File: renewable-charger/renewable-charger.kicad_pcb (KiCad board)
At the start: 2 copper layers, 150 x 40 mm, 37 parts, among them J1 Solar Input, J2 Wind Output, J3 Output, J4 USB_B_Micro, J5 Battery, M1 Stepper_Motor_bipolar, Q1 P-channel 30V 4A MOSfet, Q2 P-channel 30V 4A MOSfet, U1 CN3791

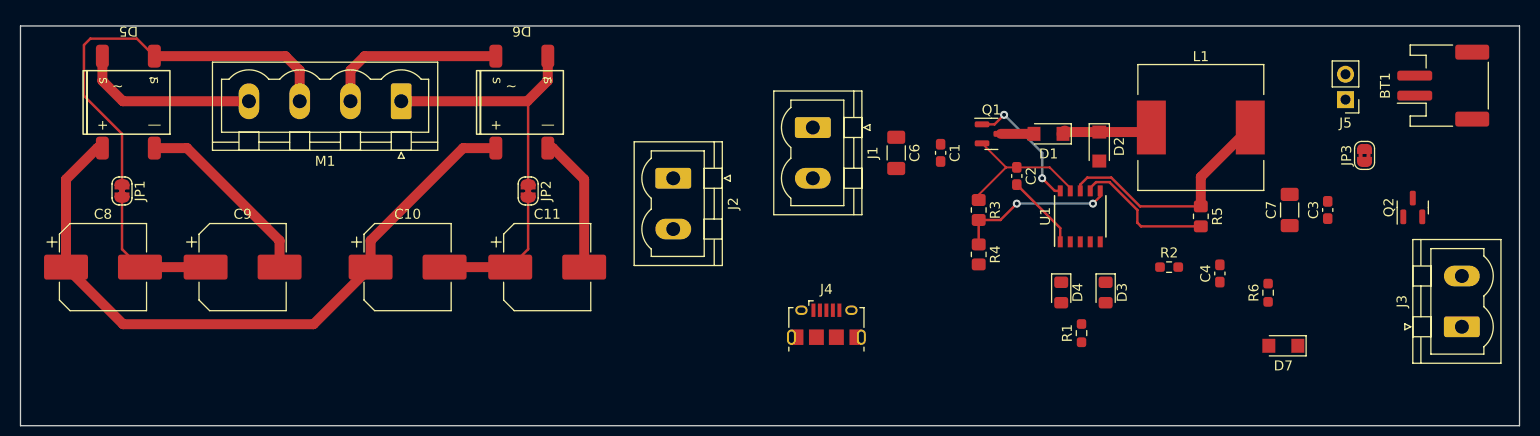
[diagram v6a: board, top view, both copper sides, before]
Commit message: All connections wired on PCB.  Still needs zones, final position for mounting holes and edges, and some labelling.  Part of #4
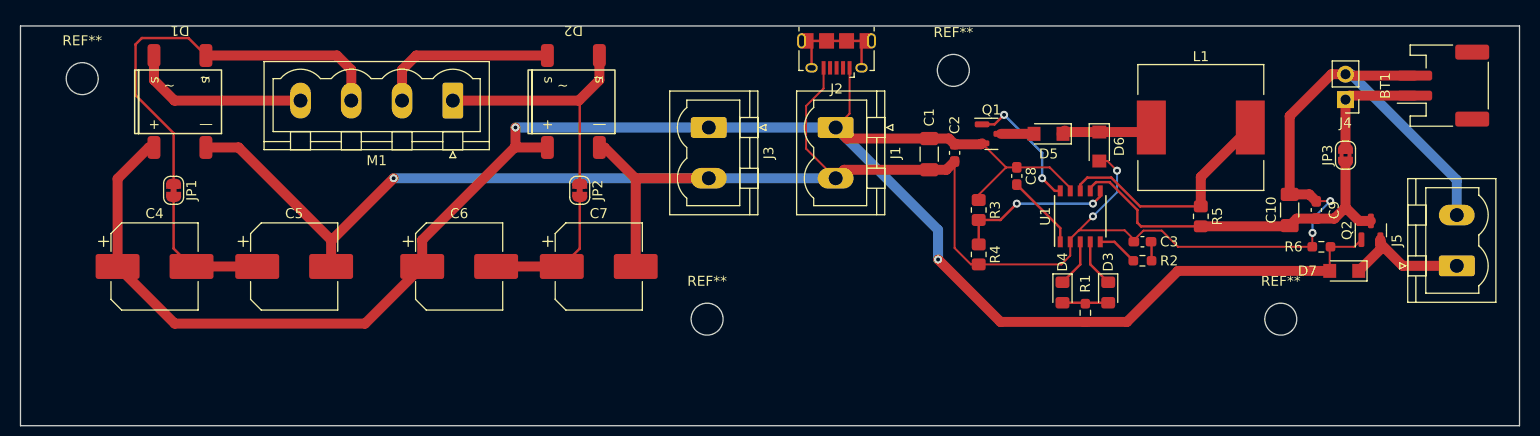
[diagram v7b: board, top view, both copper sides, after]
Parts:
- added REF**: MountingHole_3.2mm_M3_DIN965, MountingHole:MountingHole_3.2mm_M3_DIN965, F.Cu at (205.7, 64.1)
- added REF**: MountingHole_3.2mm_M3_DIN965, MountingHole:MountingHole_3.2mm_M3_DIN965, F.Cu at (181.1, 89.0)
- added REF**: MountingHole_3.2mm_M3_DIN965, MountingHole:MountingHole_3.2mm_M3_DIN965, F.Cu at (118.6, 65.0)
- added REF**: MountingHole_3.2mm_M3_DIN965, MountingHole:MountingHole_3.2mm_M3_DIN965, F.Cu at (238.5, 89.0)
- moved J2 27.1 mm to (194.1, 62.5), turned to 180 degrees
- moved D7 9.66 mm to (244.9, 84.2)
- moved C3 8.37 mm to (224.7, 81.3), turned to 180 degrees
- moved R6 7.04 mm to (242.6, 81.8), turned to 180 degrees
- moved J3 6.20 mm to (181.3, 69.8)
- moved J5 6.12 mm to (256.1, 83.7)
- moved C6 5.16 mm to (156.3, 83.8)
- moved C7 5.16 mm to (170.3, 83.8)
- moved D1 5.16 mm to (128.4, 67.2)
- moved JP2 5.16 mm to (168.4, 76.1)
- moved C4 5.16 mm to (125.8, 83.8)
- moved JP1 5.16 mm to (127.7, 76.1)
- moved C5 5.16 mm to (139.8, 83.8)
- moved D2 5.16 mm to (167.7, 67.2)
- moved M1 5.16 mm to (155.7, 67.2)
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- renumbered C6 to C1, C7 to C10, C1 to C2, C4 to C3, C8 to C4, C9 to C5, C10 to C6, C11 to C7, C2 to C8, C3 to C9, D5 to D1, D6 to D2, D1 to D5, D2 to D6, J4 to J2, J2 to J3, J5 to J4, J3 to J5
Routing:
- net /Power -: track 32.7 -> 229.0 mm, vias 0 -> 5
- net /Power +: track 83.4 -> 206.6 mm, vias 0 -> 2
- net Net-(JP3-A): track 14.2 -> 37.1 mm
- net Net-(D7-K): track 0.00 -> 13.0 mm
- net Net-(BT1-+): track 0.00 -> 12.0 mm
- net unconnected-(J2-Shield): track 0.00 -> 11.5 mm
- net Net-(D3-K): track 0.00 -> 4.79 mm
- net Net-(D4-K): track 0.00 -> 4.78 mm
- net Net-(D3-A): track 0.00 -> 4.65 mm
- net Net-(U1-COM): track 0.00 -> 4.10 mm
- net Net-(C3-Pad1): track 0.00 -> 1.93 mm

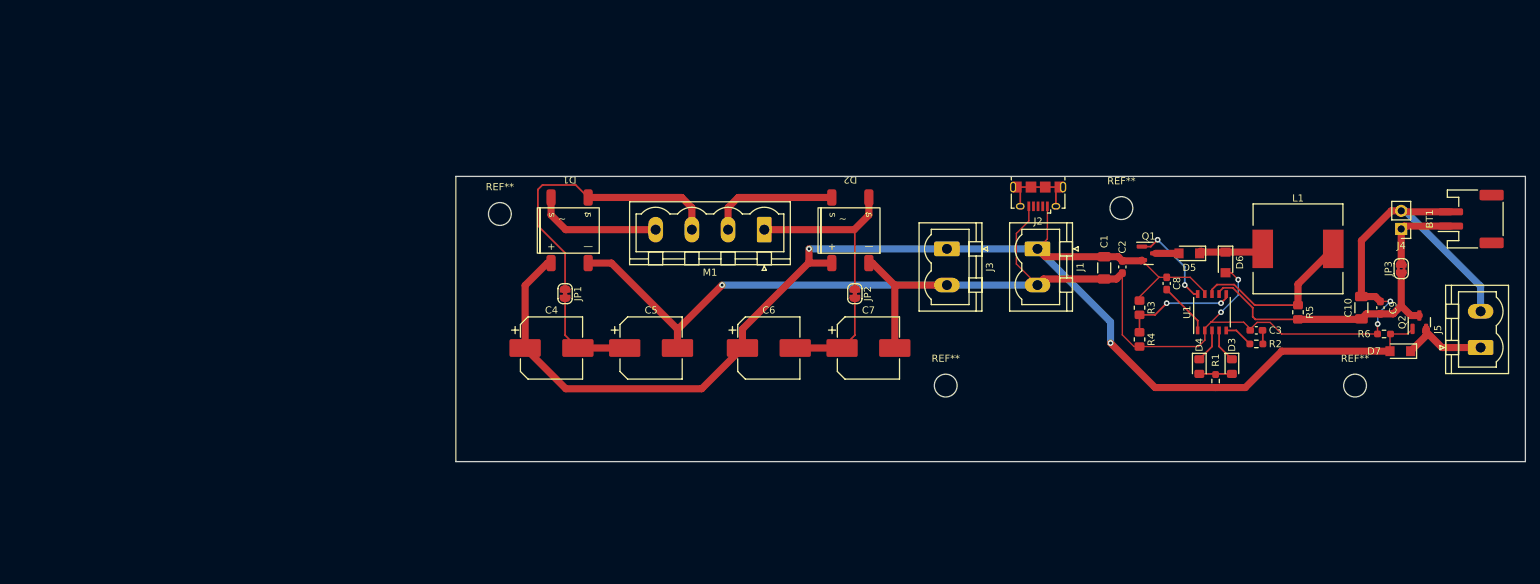
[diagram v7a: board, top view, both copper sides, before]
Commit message: Added copper zones; positioned mounting holes and tidied up edge cuts.  Just labels left.  Part of #4
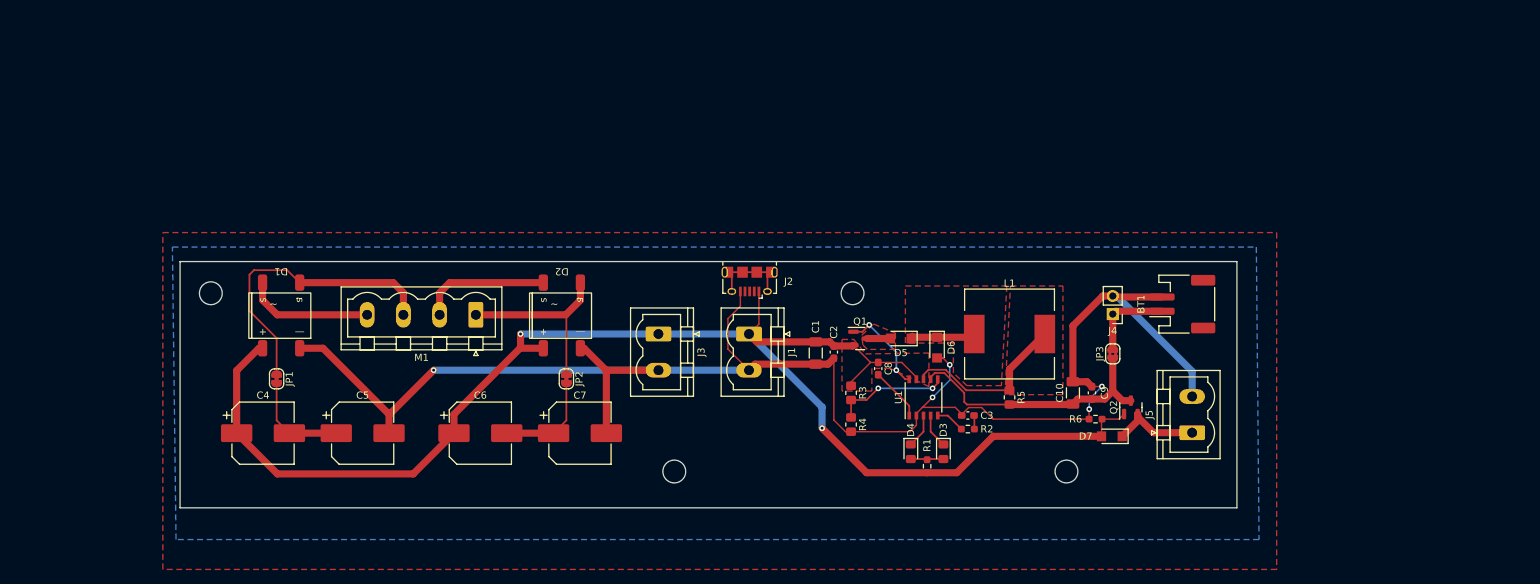
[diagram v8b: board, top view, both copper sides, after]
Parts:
- moved REF** 42.2 mm to (198.0, 101.1)
- moved J1 42.2 mm to (153.5, 81.8)
- moved C10 42.2 mm to (198.9, 90.0)
- moved C3 42.2 mm to (184.2, 93.2)
- moved C7 42.2 mm to (129.8, 95.7)
- moved C8 42.2 mm to (171.6, 86.6)
- moved C9 42.2 mm to (201.6, 90.0)
- moved D1 42.2 mm to (87.9, 79.2)
- moved D3 42.2 mm to (180.8, 98.3)
- moved D4 42.2 mm to (176.2, 98.3)
- moved J2 42.2 mm to (153.6, 74.4)
- moved J4 42.2 mm to (204.5, 79.0)
- moved J5 42.2 mm to (215.7, 95.6)
- moved JP3 42.2 mm to (204.5, 84.6)
- moved Q1 42.2 mm to (169.1, 82.4)
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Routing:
- added copper zone on F.Cu, net /Power +
- added copper zone on B.Cu, net /Power -
- added copper zone on F.Cu, net /Power -
- added copper zone on F.Cu, net Net-(D5-A)
- added copper zone on F.Cu, net Net-(D5-K)
- added copper zone on F.Cu, net Net-(U1-CSP)
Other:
- board size 150 x 40 mm -> 148.2 x 34.5 mm
